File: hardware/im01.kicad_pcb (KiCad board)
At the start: 2 copper layers, 80 x 55 mm, 110 parts, among them J1 ПИТАНИЕ 9-30В, J2 COIN, J3 BILL, J4 NANO SIM, J5 U.FL, J6 SWD, Q1 2N7002, Q2 2N7002, SW1 ВЫГРУЗКА, U1 LMR16020, U2 ME6211C33, U3 STM32G030K8T6, U4 FM25L16B, U5 EL817S1(B), U6 EL817S1(B), U7 EG800K-EU, U8 SRV05-4, U9 TXS0102

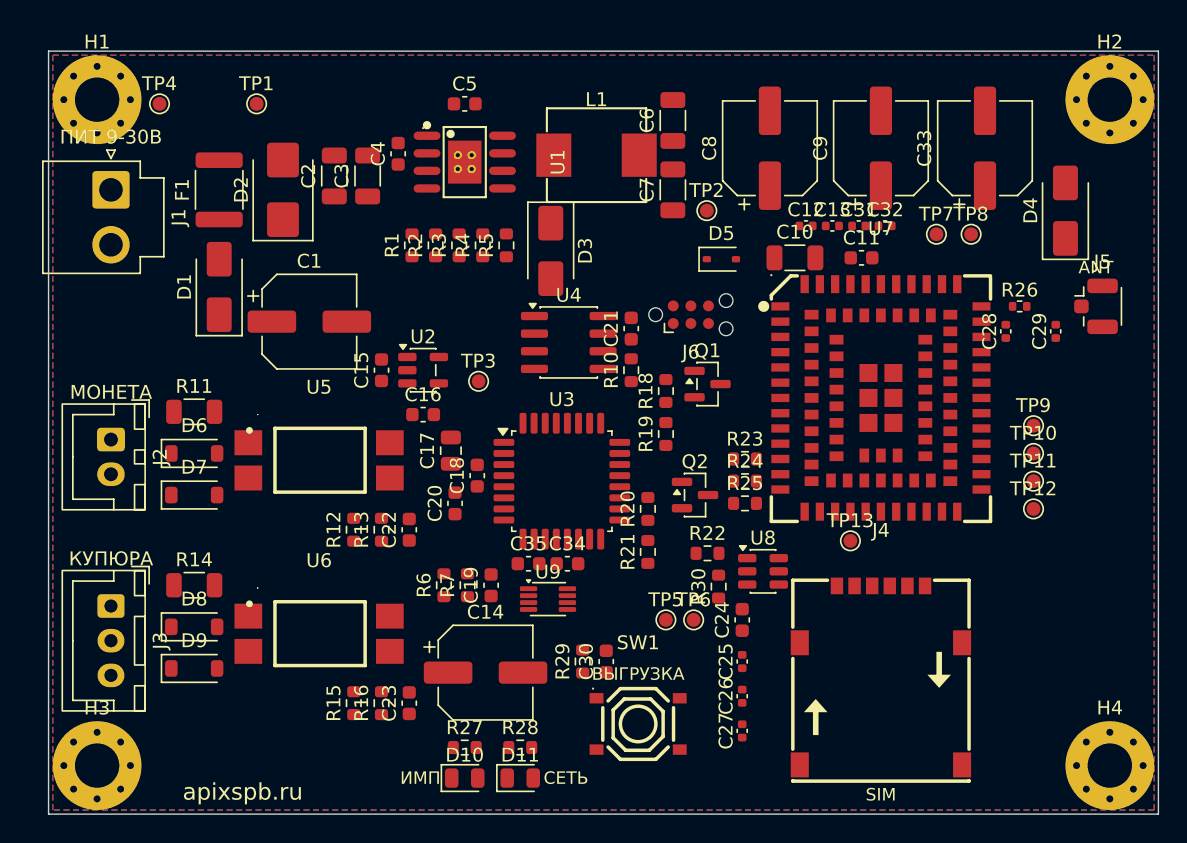
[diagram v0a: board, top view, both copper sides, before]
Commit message: feat(hardware): разводка платы ИМ-01, файлы для JLCPCB, виртуальная модель
Три критичные цепи (антенна, узел SW, путь VBAT) разведены по заданной
геометрии и зафиксированы, остальное — Freerouting; земля досоединяется
по отчёту DRC. Итог: ERC 0 ошибок, DRC 0 нарушений и 0 неподключённых,
сверка платы со схемой — 0 расхождений. fab/: гербер-архив, BOM и CPL
для JLCPCB, PDF схемы и сборочного чертежа, STEP и 3D-вид.
sim/run_final.py — модель всего устройства с окончательными номиналами:
все 5 сценариев проходят (VBAT ≥ 3.53 В, MCU живёт ~50 мс после
пропадания 12 В).

Co-Authored-By: Claude Opus 5 <noreply@anthropic.com>
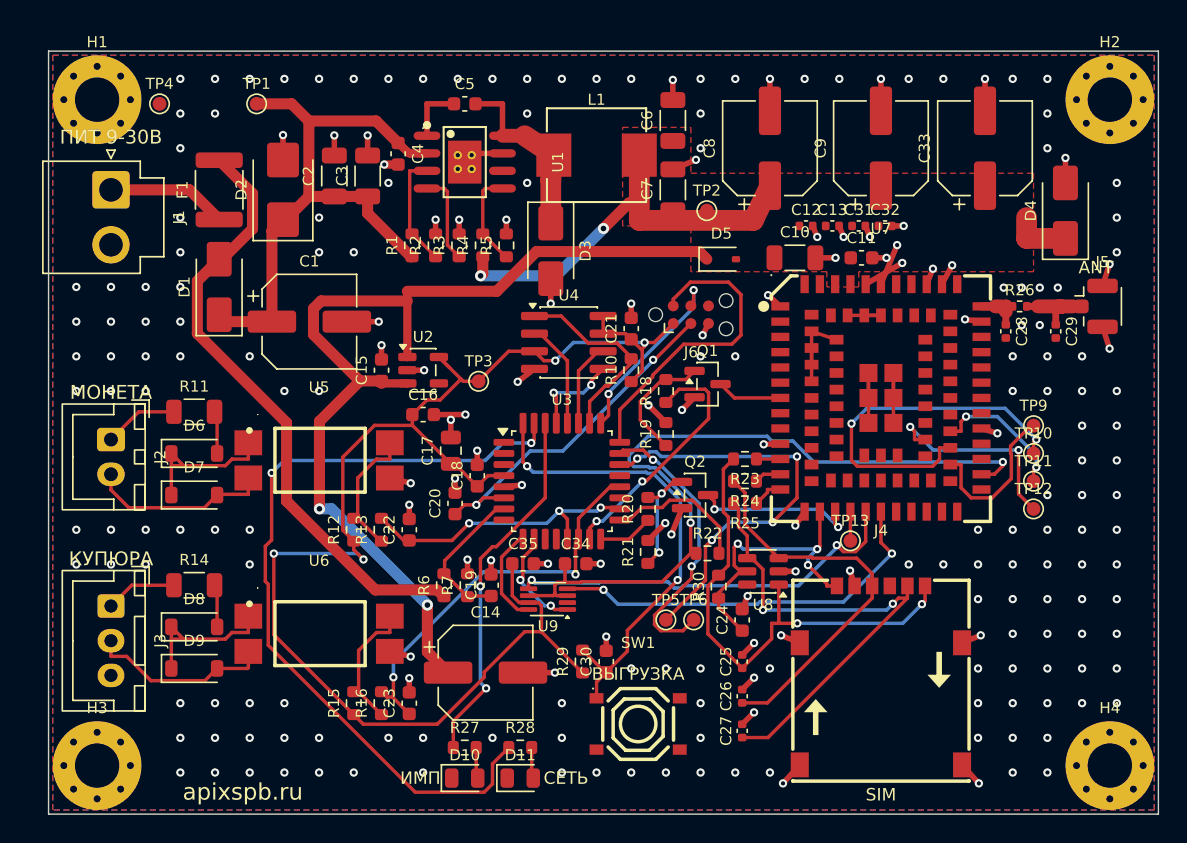
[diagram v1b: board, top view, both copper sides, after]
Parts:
- removed TP7: MODEM_DBG_TX, TestPoint:TestPoint_Pad_D1.0mm
- removed TP8: MODEM_DBG_RX, TestPoint:TestPoint_Pad_D1.0mm
- moved C34 0.60 mm to (138.0, 136.9)
- moved C35 0.40 mm to (134.2, 136.9)
- turned C28 to -90 degrees
- turned C29 to -90 degrees
- turned C4 to -90 degrees
- turned R23 to 180 degrees
- turned R24 to 180 degrees
- turned R25 to 180 degrees
- turned U8 to 180 degrees
- turned U9 to 180 degrees
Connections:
- U7 pad 38: MODEM_DBG_RX -> (no net)
- U7 pad 39: MODEM_DBG_TX -> (no net)
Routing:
- net GND: track 0.00 -> 117.4 mm, vias 0 -> 226
- net +3V3: track 0.00 -> 105.0 mm, vias 0 -> 4
- net VMCU_IN: track 0.00 -> 71.5 mm, vias 0 -> 2
- net LED_STATUS: track 0.00 -> 57.7 mm, vias 0 -> 2
- net VDD_EXT: track 0.00 -> 56.1 mm, vias 0 -> 2
- net VIN_F: track 0.00 -> 44.2 mm
- net VIN: track 0.00 -> 43.4 mm
- net SIM_DATA: track 0.00 -> 36.9 mm, vias 0 -> 2
- net SIM_CLK: track 0.00 -> 36.5 mm, vias 0 -> 2
- net VBAT: track 0.00 -> 35.0 mm, vias 0 -> 2
- net BTN: track 0.00 -> 34.4 mm, vias 0 -> 2
- net MCU_DBG_TX: track 0.00 -> 30.8 mm, vias 0 -> 4
- net BILL_IN: track 0.00 -> 29.2 mm, vias 0 -> 2
- net MODEM_RXD: track 0.00 -> 29.1 mm, vias 0 -> 2
- net MODEM_TXD: track 0.00 -> 28.7 mm, vias 0 -> 2
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- added copper zone on F.Cu, net VBAT
